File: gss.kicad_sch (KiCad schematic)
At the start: 13 parts

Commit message: Big Pluto Commit, baboucarr jeng imperial college london second year aeronautics student.
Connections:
- net at BV_Depressurise_Nitrogen1.: now also BVNitrogen1., QD2.
- net at Needle_Valve_Nitrous1.: now also BVNitrous1., NitrousTank1.
- new net: BVNitrous1., BV_Depressurise_Nitrous1., QD1.
- new net: BVNitrogen1., Needle_Valve_Nitrogen1., Nitrogen1., Reg1.
- now unconnected: BV_Depressurise_Nitrous1., Needle_Valve_Nitrogen1., Nitrogen1., NitrousTank1.
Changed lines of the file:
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@@
 (kicad_sch
-	(version 20231120)
+	(version 20250114)
 	(generator "eeschema")
-	(generator_version "8.0")
+	(generator_version "9.0")
 	(paper "A4")
 	(junction
@@
 	(label "N2_VEHICLE"
 		(at 181.61 52.07 0)
-		(fields_autoplaced yes)
 		(effects
 			(font
@@
 	(label "OX_VEHICLE"
 		(at 105.41 50.8 0)
-		(fields_autoplaced yes)
 		(effects
 			(font

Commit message: no message
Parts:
- renumbered Pmatic_B_Valve2 to Pmatic_B_Valve1, QD1 to QD4, QD2 to QD5, Reg1 to Reg3
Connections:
- net at BV_Depressurise_Nitrogen1.: now also BVNitrogen1., QD5.
- net at Needle_Valve_Nitrous1.: now also BVNitrous1., NitrousTank1.
- new net: BVNitrous1., BV_Depressurise_Nitrous1., QD4.
- new net: BVNitrogen1., Needle_Valve_Nitrogen1., Nitrogen1., Reg3.
- now unconnected: BV_Depressurise_Nitrous1., Needle_Valve_Nitrogen1., Nitrogen1., NitrousTank1.
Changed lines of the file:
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@@
 		(dnp no)
 		(fields_autoplaced yes)
-		(property "Reference" "QD1"
+		(property "Reference" "QD4"
 			(at 101.6 53.3399 90)
 			(effects
@@
 			(project "P_IDs"
 				(path "/045f1f05-3134-4b6d-91b6-463031104f1e/b22dc67f-22e2-4992-8273-fe279f768d16"
-					(reference "QD1")
-					(unit 1)
-				)
-			)
-		)
-	)
-	(symbol
+					(reference "QD4")
+					(unit 1)
+				)
+			)
+		)
+	)
+	(symbol
+		(lib_name "Ball_Valve_1")
 		(lib_id "PID_symbols:Ball_Valve")
 		(at 181.61 99.06 90)
@@
 		(dnp no)
 		(fields_autoplaced yes)
-		(property "Reference" "Reg1"
+		(property "Reference" "Reg3"
 			(at 167.7025 106.68 0)
 			(effects
@@
 			(project "P_IDs"
 				(path "/045f1f05-3134-4b6d-91b6-463031104f1e/b22dc67f-22e2-4992-8273-fe279f768d16"
-					(reference "Reg1")
+					(reference "Reg3")
 					(unit 1)
 				)
@@
 		(dnp no)
 		(fields_autoplaced yes)
-		(property "Reference" "Pmatic_B_Valve2"
-			(at 172.72 72.5168 90)
-			(effects
-				(font
-					(size 1.27 1.27)
-				)
-			)
-		)
-		(property "Value" "~"
-			(at 172.72 74.4219 90)
-			(effects
-				(font
-					(size 1.27 1.27)
-				)
+		(property "Reference" "Pmatic_B_Valve1"
+			(at 165.1 75.5649 90)
+			(effects
+				(font
+					(size 1.27 1.27)
+				)
+				(justify right)
+			)
+		)
+		(property "Value" "~"
+			(at 165.1 77.47 90)
+			(effects
+				(font
+					(size 1.27 1.27)
+				)
+				(justify right)
 			)
 		)
@@
 		(pin ""
 		)
-		(pin ""
-		)
-		(instances
-			(project "P_IDs"
-				(path "/045f1f05-3134-4b6d-91b6-463031104f1e/b22dc67f-22e2-4992-8273-fe279f768d16"
-					(reference "Pmatic_B_Valve2")
-					(unit 1)
-				)
-			)
-		)
-	)
-	(symbol
+		(instances
+			(project "P_IDs"
+				(path "/045f1f05-3134-4b6d-91b6-463031104f1e/b22dc67f-22e2-4992-8273-fe279f768d16"
+					(reference "Pmatic_B_Valve1")
+					(unit 1)
+				)
+			)
+		)
+	)
+	(symbol
+		(lib_name "Needle_Valve_1")
 		(lib_id "PID_symbols:Needle_Valve")
 		(at 187.96 109.22 0)
@@
 	)
 	(symbol
+		(lib_name "Ball_Valve_2")
 		(lib_id "PID_symbols:Ball_Valve")
 		(at 105.41 97.79 90)
@@
 	)
 	(symbol
+		(lib_name "Quick_Disconnect_1")
 		(lib_id "PID_symbols:Quick_Disconnect")
 		(at 181.61 55.88 90)
@@
 		(dnp no)
 		(fields_autoplaced yes)
-		(property "Reference" "QD2"
+		(property "Reference" "QD5"
 			(at 177.8 54.6099 90)
 			(effects
@@
 			(project "P_IDs"
 				(path "/045f1f05-3134-4b6d-91b6-463031104f1e/b22dc67f-22e2-4992-8273-fe279f768d16"
-					(reference "QD2")
-					(unit 1)
-				)
-			)
-		)
-	)
-	(symbol
+					(reference "QD5")
+					(unit 1)
+				)
+			)
+		)
+	)
+	(symbol
+		(lib_name "Tank_1")
 		(lib_id "PID_symbols:Tank")
 		(at 104.14 133.35 0)
@@
 	)
 	(symbol
+		(lib_name "Ball_Valve_3")
 		(lib_id "PID_symbols:Ball_Valve")
 		(at 115.57 66.04 90)

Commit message: added universal key
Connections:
- net at BV_Depressurise_Nitrogen1.: now also BVNitrogen1., QD5.
- net at Needle_Valve_Nitrous1.: now also BVNitrous1., NitrousTank1.
- new net: BVNitrous1., BV_Depressurise_Nitrous1., QD4.
- new net: BVNitrogen1., Needle_Valve_Nitrogen1., Nitrogen1., Reg3.
- now unconnected: BV_Depressurise_Nitrous1., Needle_Valve_Nitrogen1., Nitrogen1., NitrousTank1.
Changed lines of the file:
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@@
+		(pin ""
+		)
 		(pin ""
 		)

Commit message: gss
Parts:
- added CV16, CV17: ~, symbol PID_symbols:Check_Valve
- added H1, Hose: ~, symbol PID_symbols:Hose
- added MB_V7: ~, symbol PID_symbols:MBallValve
- added NitrousTank2: ~, symbol PID_symbols:Tank
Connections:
- net at BV_Depressurise_Nitrogen1.: now also BVNitrogen1., QD5.
- net at Needle_Valve_Nitrous1.: now also BVNitrous1., H1.1
- new net: BVNitrous1., BV_Depressurise_Nitrous1., QD4.
- new net: BVNitrogen1., Hose.1, MB_V7., Needle_Valve_Nitrogen1.
- new net: CV16., CV17., H1.2
- new net: CV16., NitrousTank2.
- new net: MB_V7., Reg3.
- new net: Hose.2, Nitrogen1.
- new net: CV17., NitrousTank1.
- now unconnected: BV_Depressurise_Nitrous1., Needle_Valve_Nitrogen1., Nitrogen1., NitrousTank1.
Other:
- moved on the sheet: Nitrogen1, NitrousTank1, Pmatic_B_Valve1, Pn_Sol2, Reg3

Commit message: no message
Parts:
- added BV10, BV9: ~, symbol PID_symbols:Ball_Valve
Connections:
- net at BV_Depressurise_Nitrogen1.: now also BVNitrogen1., QD5.
- net at Needle_Valve_Nitrous1.: now also BVNitrous1., H1.1
- net at NitrousTank2.: now also CV16.
- net at CV16.: now also BV9.; no longer NitrousTank2.
- new net: BVNitrous1., BV_Depressurise_Nitrous1., QD4.
- new net: BV10., BV9., H1.2
- new net: BV10., CV17.
- now unconnected: BV_Depressurise_Nitrous1.
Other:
- moved on the sheet: CV16, CV17, NitrousTank1, NitrousTank2
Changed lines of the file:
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@@
 	(wire
 		(pts
-			(xy 114.3 134.62) (xy 114.3 137.16)
+			(xy 114.3 147.32) (xy 114.3 151.13)
 		)
 		(stroke
@@
 	(wire
 		(pts
-			(xy 95.25 134.62) (xy 95.25 137.16)
+			(xy 95.25 147.32) (xy 95.25 151.13)
 		)
 		(stroke
@@
 		(lib_name "Tank_2")
 		(lib_id "PID_symbols:Tank")
-		(at 93.98 148.59 0)
+		(at 93.98 162.56 0)
 		(unit 1)
 		(exclude_from_sim no)
@@
 		(dnp no)
 		(property "Reference" "NitrousTank2"
-			(at 76.2 143.51 0)
-			(effects
-				(font
-					(size 1.27 1.27)
-				)
-				(justify left)
-			)
-		)
-		(property "Value" "~"
-			(at 100.33 145.415 0)
-			(effects
-				(font
-					(size 1.27 1.27)
-				)
-				(justify left)
-			)
-		)
-		(property "Footprint" ""
-			(at 93.98 148.59 0)
-			(effects
-				(font
-					(size 1.27 1.27)
-				)
-				(hide yes)
-			)
-		)
-		(property "Datasheet" ""
-			(at 93.98 148.59 0)
-			(effects
-				(font
-					(size 1.27 1.27)
-				)
-				(hide yes)
-			)
-		)
-		(property "Description" ""
-			(at 93.98 148.59 0)
+			(at 76.2 157.48 0)
+			(effects
+				(font
+					(size 1.27 1.27)
+				)
+				(justify left)
+			)
+		)
+		(property "Value" "~"
+			(at 100.33 159.385 0)
+			(effects
+				(font
+					(size 1.27 1.27)
+				)
+				(justify left)
+			)
+		)
+		(property "Footprint" ""
+			(at 93.98 162.56 0)
+			(effects
+				(font
+					(size 1.27 1.27)
+				)
+				(hide yes)
+			)
+		)
+		(property "Datasheet" ""
+			(at 93.98 162.56 0)
+			(effects
+				(font
+					(size 1.27 1.27)
+				)
+				(hide yes)
+			)
+		)
+		(property "Description" ""
+			(at 93.98 162.56 0)
 			(effects
 				(font
@@
 	)
 	(symbol
+		(lib_name "Ball_Valve_4")
+		(lib_id "PID_symbols:Ball_Valve")
+		(at 95.25 134.62 90)
+		(unit 1)
+		(exclude_from_sim no)
+		(in_bom yes)
+		(on_board yes)
+		(dnp no)
+		(fields_autoplaced yes)
+		(property "Reference" "BV9"
+			(at 99.06 130.1749 90)
+			(effects
+				(font
+					(size 1.27 1.27)
+				)
+				(justify right)
+			)
+		)
+		(property "Value" "~"
+			(at 99.06 132.08 90)
+			(effects
+				(font
+					(size 1.27 1.27)
+				)
+				(justify right)
+			)
+		)
+		(property "Footprint" ""
+			(at 95.25 134.62 0)
+			(effects
+				(font
+					(size 1.27 1.27)
+				)
+				(hide yes)
+			)
+		)
+		(property "Datasheet" ""
+			(at 95.25 134.62 0)
+			(effects
+				(font
+					(size 1.27 1.27)
+				)
+				(hide yes)
+			)
+		)
+		(property "Description" ""
+			(at 95.25 134.62 0)
+			(effects
+				(font
+					(size 1.27 1.27)
+				)
+				(hide yes)
+			)
+		)
+		(pin ""
+		)
+		(pin ""
+		)
+		(instances
+			(project ""
+				(path "/045f1f05-3134-4b6d-91b6-463031104f1e/b22dc67f-22e2-4992-8273-fe279f768d16"
+					(reference "BV9")
+					(unit 1)
+				)
+			)
+		)
+	)
+	(symbol
 		(lib_id "PID_symbols:Pneumatic_Rotary_Ball_Valve")
 		(at 154.94 76.2 90)
@@
 				(path "/045f1f05-3134-4b6d-91b6-463031104f1e/b22dc67f-22e2-4992-8273-fe279f768d16"
 					(reference "Pmatic_B_Valve1")
+					(unit 1)
+				)
+			)
+		)
+	)
+	(symbol
+		(lib_name "Ball_Valve_5")
+		(lib_id "PID_symbols:Ball_Valve")
+		(at 114.3 134.62 90)
+		(unit 1)
+		(exclude_from_sim no)
+		(in_bom yes)
+		(on_board yes)
+		(dnp no)
+		(fields_autoplaced yes)
+		(property "Reference" "BV10"
+			(at 118.11 130.1749 90)
+			(effects
+				(font
+					(size 1.27 1.27)
+				)
+				(justify right)
+			)
+		)
+		(property "Value" "~"
+			(at 118.11 132.08 90)
+			(effects
+				(font
+					(size 1.27 1.27)
+				)
+				(justify right)
+			)
+		)
+		(property "Footprint" ""
+			(at 114.3 134.62 0)
+			(effects
+				(font
+					(size 1.27 1.27)
+				)
+				(hide yes)
+			)
+		)
+		(property "Datasheet" ""
+			(at 114.3 134.62 0)
+			(effects
+				(font
+					(size 1.27 1.27)
+				)
+				(hide yes)
+			)
+		)
+		(property "Description" ""
+			(at 114.3 134.62 0)
+			(effects
+				(font
+					(size 1.27 1.27)
+				)
+				(hide yes)
+			)
+		)
+		(pin ""
+		)
+		(pin ""
+		)
+		(instances
+			(project "P_IDs"
+				(path "/045f1f05-3134-4b6d-91b6-463031104f1e/b22dc67f-22e2-4992-8273-fe279f768d16"
+					(reference "BV10")
 					(unit 1)
 				)
@@
 		(lib_name "Check_Valve_1")
 		(lib_id "PID_symbols:Check_Valve")
-		(at 114.3 132.08 90)
+		(at 114.3 144.78 90)
 		(unit 1)
 		(exclude_from_sim no)
@@
 		(fields_autoplaced yes)
 		(property "Reference" "CV17"
-			(at 118.11 129.0319 90)
+			(at 118.11 141.7319 90)
 			(effects
 				(font
@@
 		)
 		(property "Value" "~"
-			(at 118.11 130.937 90)
+			(at 118.11 143.637 90)
 			(effects
 				(font
@@
 		)
 		(property "Footprint" ""
-			(at 114.3 132.08 0)
-			(effects
-				(font
-					(size 1.27 1.27)
-				)
-				(hide yes)
-			)
-		)
-		(property "Datasheet" ""
-			(at 114.3 132.08 0)
-			(effects
-				(font
-					(size 1.27 1.27)
-				)
-				(hide yes)
-			)
-		)
-		(property "Description" ""
-			(at 114.3 132.08 0)
+			(at 114.3 144.78 0)
+			(effects
+				(font
+					(size 1.27 1.27)
+				)
+				(hide yes)
+			)
+		)
+		(property "Datasheet" ""
+			(at 114.3 144.78 0)
+			(effects
+				(font
+					(size 1.27 1.27)
+				)
+				(hide yes)
+			)
+		)
+		(property "Description" ""
+			(at 114.3 144.78 0)
 			(effects
 				(font
@@
 		(lib_name "Tank_1")
 		(lib_id "PID_symbols:Tank")
-		(at 113.03 148.59 0)
+		(at 113.03 162.56 0)
 		(unit 1)
 		(exclude_from_sim no)
@@
 		(fields_autoplaced yes)
 		(property "Reference" "NitrousTank1"
-			(at 119.38 143.5099 0)
-			(effects
-				(font
-					(size 1.27 1.27)
-				)
-				(justify left)
-			)
-		)
-		(property "Value" "~"
-			(at 119.38 145.415 0)
-			(effects
-				(font
-					(size 1.27 1.27)
-				)
-				(justify left)
-			)
-		)
-		(property "Footprint" ""
-			(at 113.03 148.59 0)
-			(effects
-				(font
-					(size 1.27 1.27)
-				)
-				(hide yes)
-			)
-		)
-		(property "Datasheet" ""
-			(at 113.03 148.59 0)
-			(effects
-				(font
-					(size 1.27 1.27)
-				)
-				(hide yes)
-			)
-		)
-		(property "Description" ""
-			(at 113.03 148.59 0)
+			(at 119.38 157.4799 0)
+			(effects
+				(font
+					(size 1.27 1.27)
+				)
+				(justify left)
+			)
+		)
+		(property "Value" "~"
+			(at 119.38 159.385 0)
+			(effects
+				(font
+					(size 1.27 1.27)
+				)
+				(justify left)
+			)
+		)
+		(property "Footprint" ""
+			(at 113.03 162.56 0)
+			(effects
+				(font
+					(size 1.27 1.27)
+				)
+				(hide yes)
+			)
+		)
+		(property "Datasheet" ""
+			(at 113.03 162.56 0)
+			(effects
+				(font
+					(size 1.27 1.27)
+				)
+				(hide yes)
+			)
+		)
+		(property "Description" ""
+			(at 113.03 162.56 0)
 			(effects
 				(font
@@
 	(symbol
 		(lib_id "PID_symbols:Check_Valve")
-		(at 95.25 132.08 90)
+		(at 95.25 144.78 90)
 		(unit 1)
 		(exclude_from_sim no)
@@
 		(fields_autoplaced yes)
 		(property "Reference" "CV16"
-			(at 99.06 129.0319 90)
+			(at 99.06 141.7319 90)
 			(effects
 				(font
@@
 		)
 		(property "Value" "~"
-			(at 99.06 130.937 90)
+			(at 99.06 143.637 90)
 			(effects
 				(font
@@
 		)
 		(property "Footprint" ""
-			(at 95.25 132.08 0)
-			(effects
-				(font
-					(size 1.27 1.27)
-				)
-				(hide yes)
-			)
-		)
-		(property "Datasheet" ""
-			(at 95.25 132.08 0)
-			(effects
-				(font
-					(size 1.27 1.27)
-				)
-				(hide yes)
-			)
-		)
-		(property "Description" ""
-			(at 95.25 132.08 0)
-			(effects
-				(font
+			(at 95.25 144.78 0)
+			(effects
+				(font
+					(size 1.27 1.27)
+				)
+				(hide yes)
+			)
+		)
+		(property "Datasheet" ""
+			(at 95.25 144.78 0)
+			(effects
+				(font
+					(size 1.27 1.27)
+				)
+				(hide yes)
+			)
+		)
+		(property "Description" ""
+			(at 95.25 144.78 0)
+			(effects
+				(font

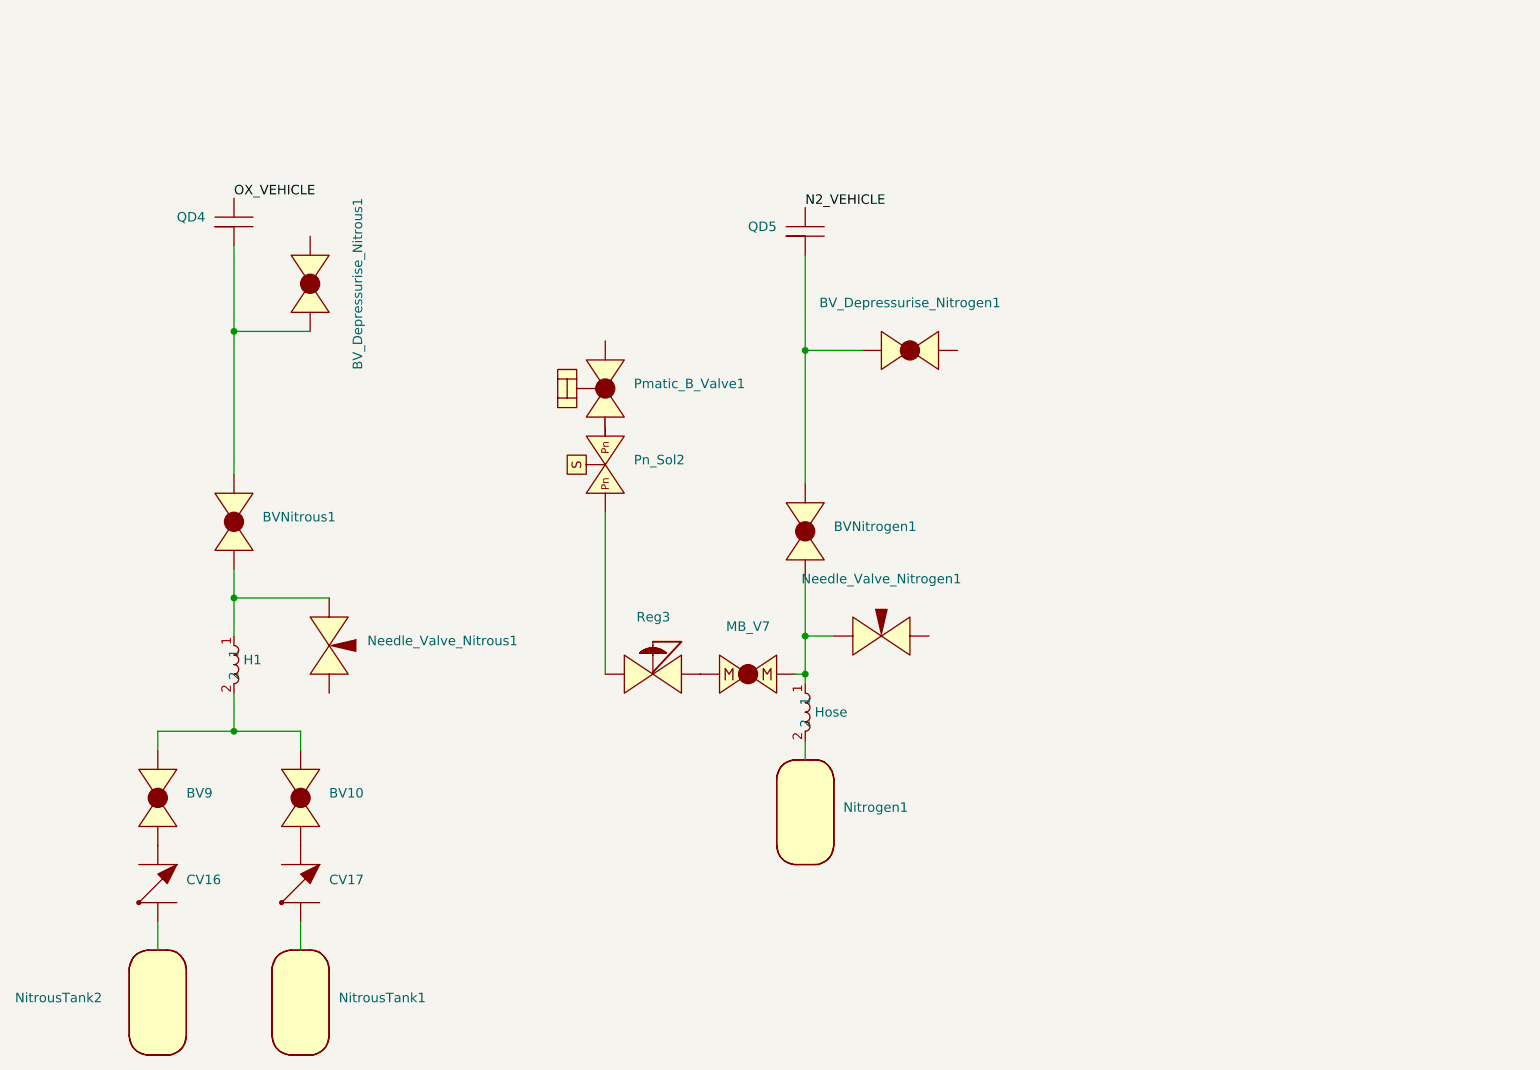
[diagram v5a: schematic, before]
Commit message: cleanup cos i was bored and procastinating. mini tutorial on defining pipe sizes in the p&id.
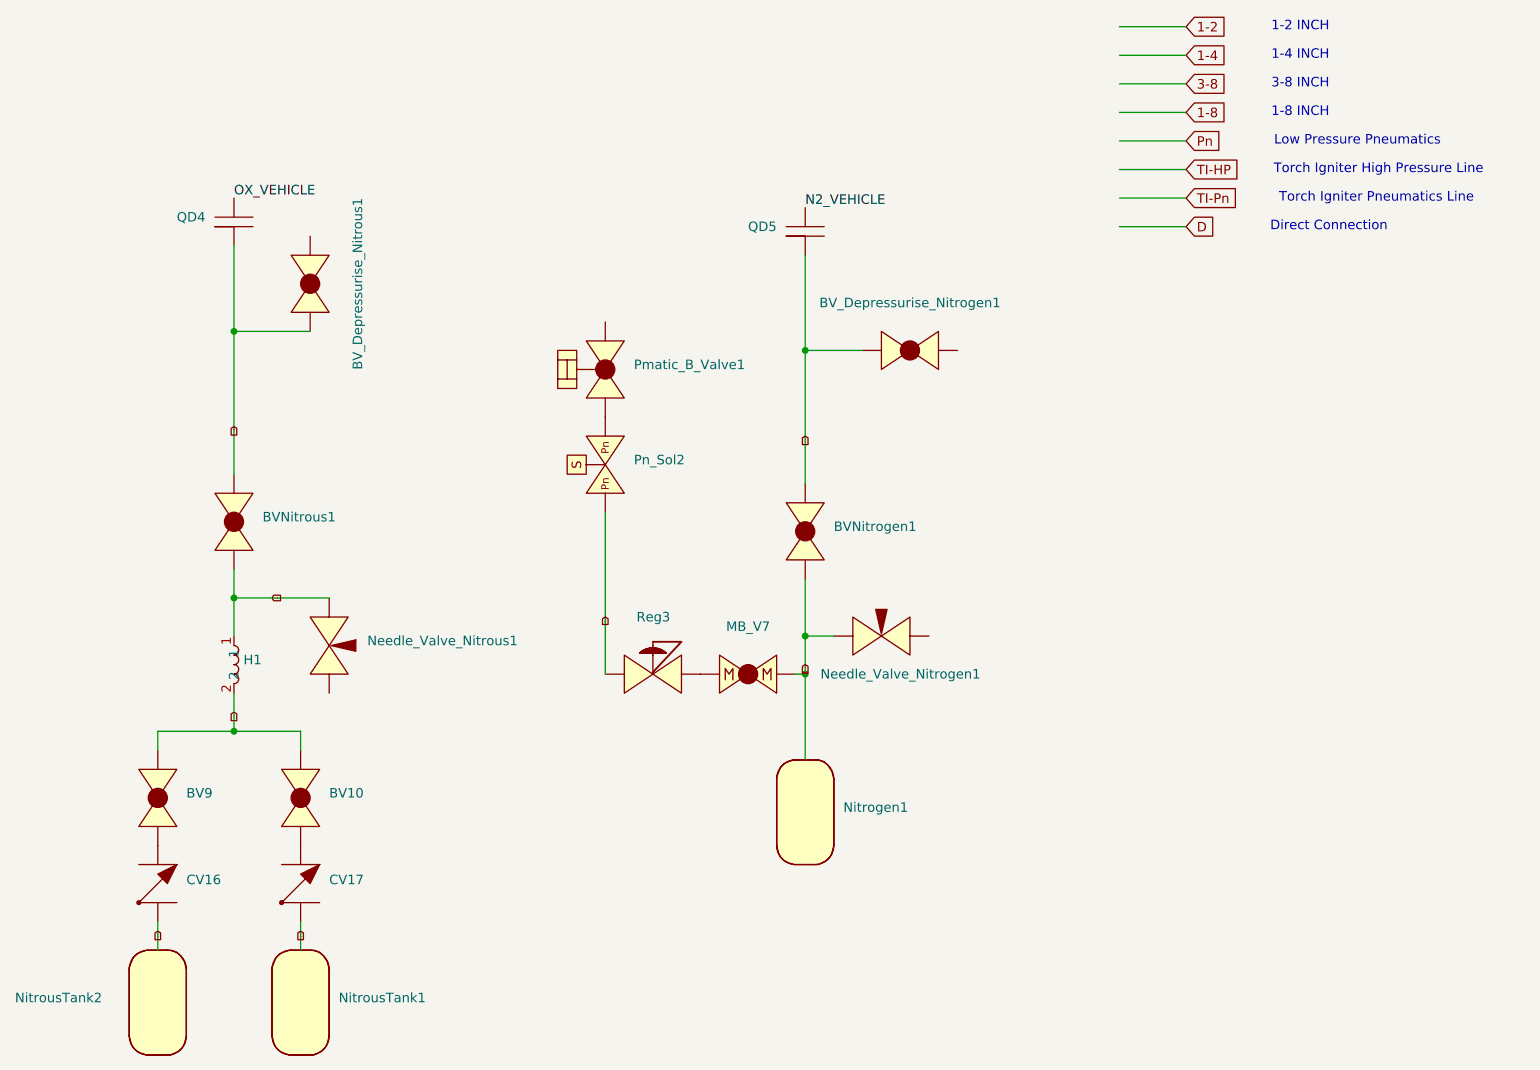
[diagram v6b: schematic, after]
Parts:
- removed Hose: ~, symbol PID_symbols:Hose
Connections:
- net 1-4: now reaches BV_Depressurise_Nitrogen1.
- net 1-4: now also BV10., BV9., BVNitrogen1., BVNitrous1., BV_Depressurise_Nitrous1., CV16., CV17., H1.1, H1.2, MB_V7., Needle_Valve_Nitrogen1., Needle_Valve_Nitrous1., Nitrogen1., NitrousTank1., NitrousTank2., QD4., QD5.
- net Pn: now reaches Reg3.
- net Pn: now also Pn_Sol2.; no longer MB_V7.
- net at Pmatic_B_Valve1.: now also Pn_Sol2.
- new net: MB_V7., Reg3.
- new net: BV9., CV16.
- new net: BV10., CV17.
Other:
- note added: "1-2 INCH"
- note added: "1-4 INCH"
- note added: "1-8 INCH"
- note added: "3-8 INCH"
- note added: "Direct Connection"
- note added: "Low Pressure Pneumatics"
- note added: "Torch Igniter High Pressure Line"
- note added: "Torch Igniter Pneumatics Line"
- moved on the sheet: Pmatic_B_Valve1
